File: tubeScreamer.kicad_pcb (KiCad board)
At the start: 2 copper layers, 100 x 100 mm, 51 parts, among them J1 IN, J2 IN, J3 OUT, J4 9V IN, J5 OUT, Q1 MMBT2222A, Q2 MMBT2222A, U1 TL072, U2 TL072

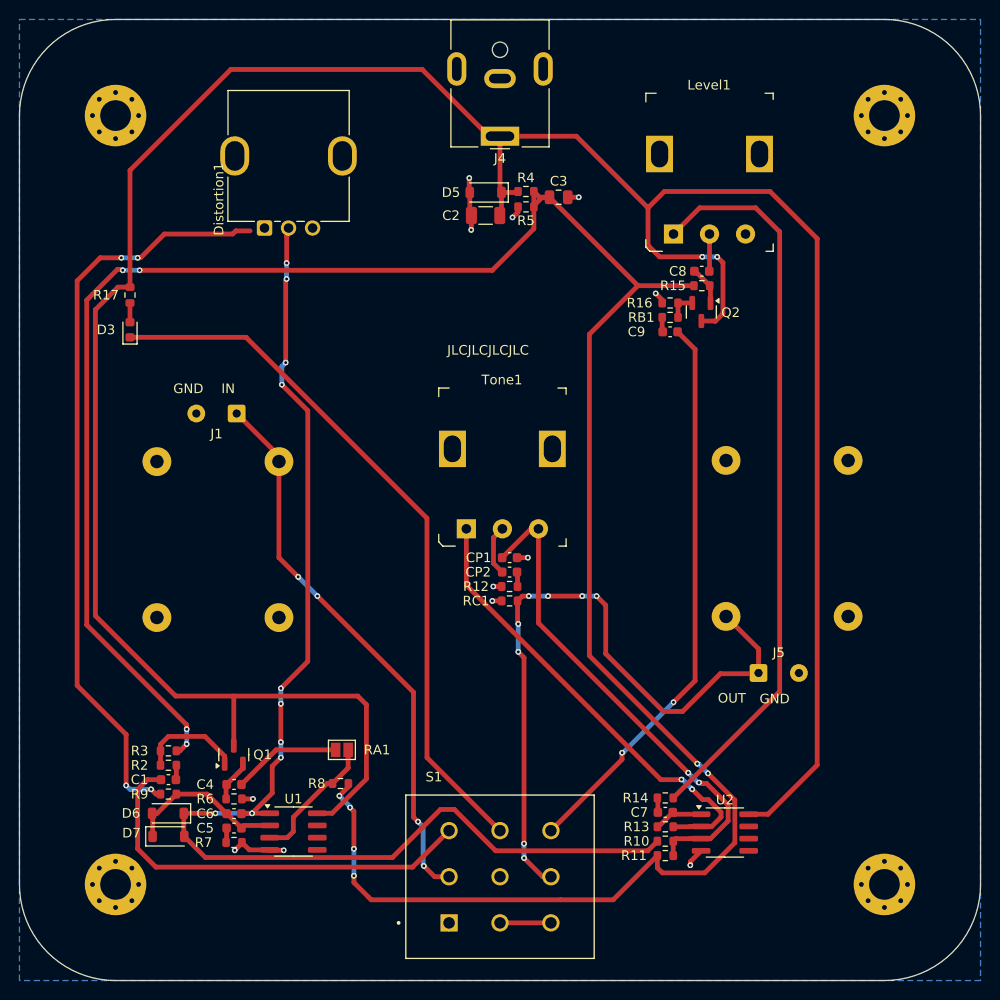
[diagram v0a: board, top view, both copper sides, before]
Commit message: updated schematic and PCB layout, 70 x 100 size, updated footprints of footswitch, Barrel Conn, audio jacks, LED and Pots, 9v Battery Compatable, corrected pot polarity, Power is cut at switch, No more 0 ohm Resister.
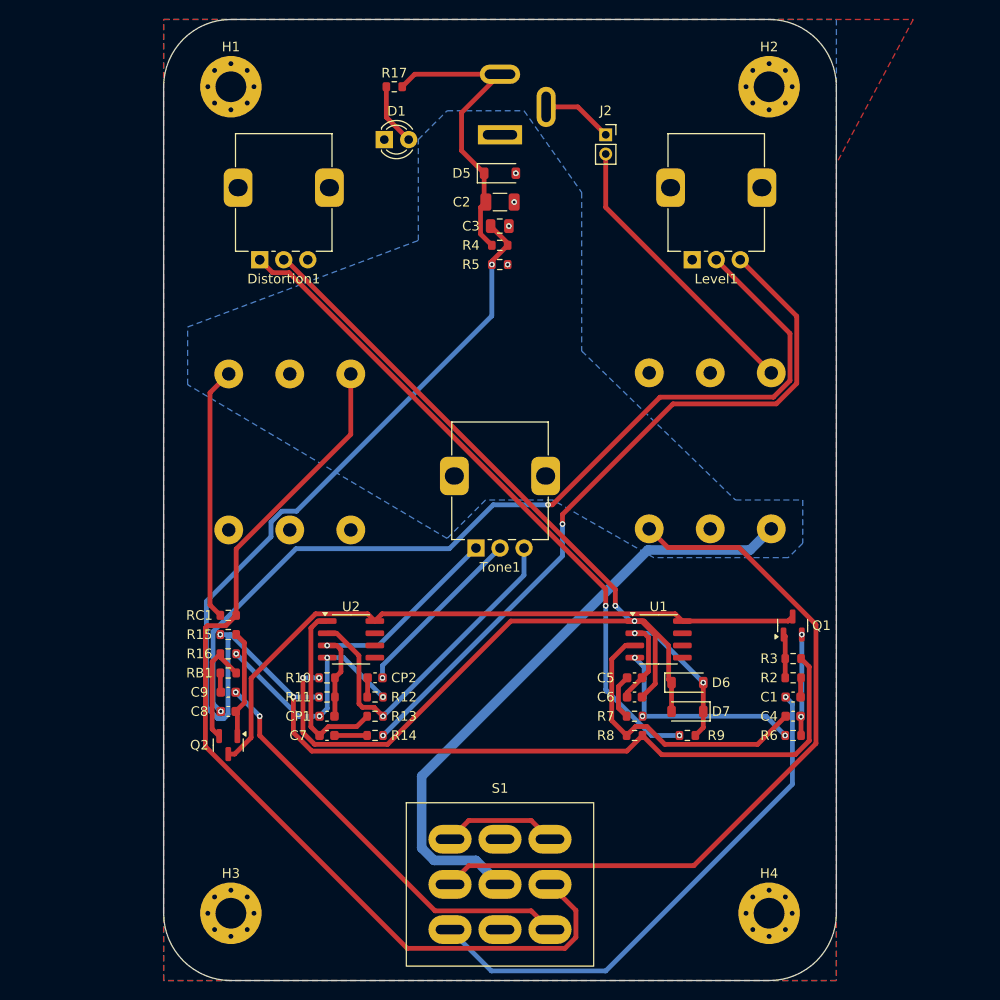
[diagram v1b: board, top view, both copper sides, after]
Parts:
- removed D3: LED, LED_SMD:LED_0603_1608Metric
- removed J3: OUT, Connector_Audio:Jack_6.35mm_Neutrik_NMJ4HFD2_Horizontal
- removed RA1: 0, Jumper:SolderJumper-2_P1.3mm_Open_Pad1.0x1.5mm
- added D1: LED, LED_THT:LED_D3.0mm_Clear, F.Cu at (138.0, 62.5)
- Distortion1: footprint Rotary_Encoder:RotaryEncoder_Bourns_Vertical_PEC12R-3x17F-Nxxxx -> Potentiometer_THT:Potentiometer_RK097_Single_Vertical
- J1: value IN -> DC IN; footprint Connector_Wire:SolderWire-0.25sqmm_1x02_P4.2mm_D0.65mm_OD1.7mm -> Connector_BarrelJack:BarrelJack_GCT_DCJ200-10-A_Horizontal; moved to B.Cu
- J2: value IN -> 9V battery; footprint Connector_Audio:Jack_6.35mm_Neutrik_NMJ4HFD2_Horizontal -> Connector_PinSocket_2.00mm:PinSocket_1x02_P2.00mm_Vertical; moved to F.Cu
- J4: value 9V IN -> IN; footprint Connector_BarrelJack:BarrelJack_CUI_PJ-063AH_Horizontal -> Connector_Audio:Jack_6.35mm_Neutrik_NMJ6HFD2_Horizontal; moved to B.Cu
- J5: footprint Connector_Wire:SolderWire-0.25sqmm_1x02_P4.2mm_D0.65mm_OD1.7mm -> Connector_Audio:Jack_6.35mm_Neutrik_NMJ6HFD2_Horizontal; moved to B.Cu
- Level1, Tone1: footprint digikey-footprints:Potentiometer_P120PK-Y25BR10K -> Potentiometer_THT:Potentiometer_RK097_Single_Vertical
- R17: value 1k -> 350
- S1: footprint FS57003PLT2B2M2QE:SW_FS57003PLT2B2M2QE -> Button_Switch_THT:3PDT Foot Switch
- moved C8 67.3 mm to (121.7, 122.0), turned to 0 degrees
- moved Q2 66.7 mm to (121.7, 125.5)
- moved R3 65.7 mm to (180.5, 116.5)
- moved R2 65.6 mm to (180.5, 118.5)
- moved C1 65.6 mm to (180.5, 120.5)
- moved R15 61.2 mm to (121.7, 114.0)
- moved Q1 59.7 mm to (180.4, 113.1)
- moved C9 59.3 mm to (121.7, 120.0)
- moved RB1 59.0 mm to (121.7, 118.0)
- moved R16 58.7 mm to (121.7, 116.0), turned to 0 degrees
- moved C4 58.6 mm to (180.5, 122.5), turned to 180 degrees
- moved R6 58.5 mm to (180.5, 124.5), turned to 0 degrees
- moved D6 55.7 mm to (169.5, 119.0), turned to 0 degrees
- moved D7 55.5 mm to (169.5, 122.0), turned to 180 degrees
- moved R9 54.3 mm to (169.5, 124.5)
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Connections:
- CP1 pad 2: GND -> 0V
- J1 pad 1: IN -> GND
- J1 pad 2: GND -> 9V
- Level1 pad 1: Net-(Level1-Pad1) -> 0V
- Level1 pad 3: GND -> Net-(Level1-Pad3)
- R12 pad 1: GND -> 0V
- R14 pad 2: Net-(Level1-Pad1) -> Net-(Level1-Pad3)
- R16 pad 2: GND -> 0V
- R6 pad 1: GND -> 0V
- R7 pad 1: GND -> 0V
- R8 pad 2: Net-(R8-Pad2) -> Net-(C4-Pad2)
- S1 pad 1: unconnected-(S1-Pad1) -> Net-(S1-Pad1)
- S1 pad 4: Net-(S1-Pad4) -> unconnected-(S1-Pad4)
- S1 pad 6: Net-(D3-K) -> 0V
- S1 pad 7: Net-(S1-Pad4) -> Net-(S1-Pad1)
- Tone1 pad 1: Net-(R13-Pad1) -> Net-(CP1-Pad1)
- Tone1 pad 3: Net-(CP1-Pad1) -> Net-(R13-Pad1)
- U1 pad 3: Net-(R8-Pad2) -> Net-(C4-Pad2)
- U1 pad 4: GND -> 0V
- U2 pad 4: GND -> 0V
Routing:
- net 9V: track 279.2 -> 101.2 mm, vias 2 -> 0
- net 4.5V: track 251.0 -> 158.0 mm, vias 10 -> 4
- net Net-(C8-Pad1): track 3.89 -> 95.2 mm, vias 0 -> 2
- net Net-(Level1-Pad1): track 76.7 -> 0.00 mm
- net Net-(Level1-Pad3): track 0.00 -> 76.1 mm, vias 0 -> 2
- net Net-(D3-K): track 74.3 -> 0.00 mm
- net GND: track 21.4 -> 90.6 mm, vias 12 -> 4
- net 0V: track 0.00 -> 47.3 mm, vias 0 -> 7
- net /-ve: track 0.00 -> 29.9 mm
- net OUT: track 72.8 -> 100.5 mm, vias 8 -> 0
- net Net-(CP1-Pad1): track 52.2 -> 28.4 mm, vias 2 -> 1
- net Net-(C4-Pad2): track 11.3 -> 30.5 mm
- net IN: track 58.8 -> 78.0 mm, vias 4 -> 0
- net Net-(C7-Pad1): track 4.14 -> 19.3 mm
- net Net-(C9-Pad2): track 58.9 -> 44.1 mm
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- added copper zone on B.Cu, net 0V
- added copper zone on F.Cu, net 9V
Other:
- board size 100 x 100 mm -> 70 x 100 mm
- board text removed: "GND"
- board text removed: "IN"
- board text removed: "JLCJLCJLCJLC"
- board text removed: "OUT"
